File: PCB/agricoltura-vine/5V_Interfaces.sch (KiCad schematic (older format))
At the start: 13 parts, among them T19 TSW-108-07-G-T, T20 TSW-108-07-G-T, U8 SN74LV541APWR, U9 TXB0108PWR

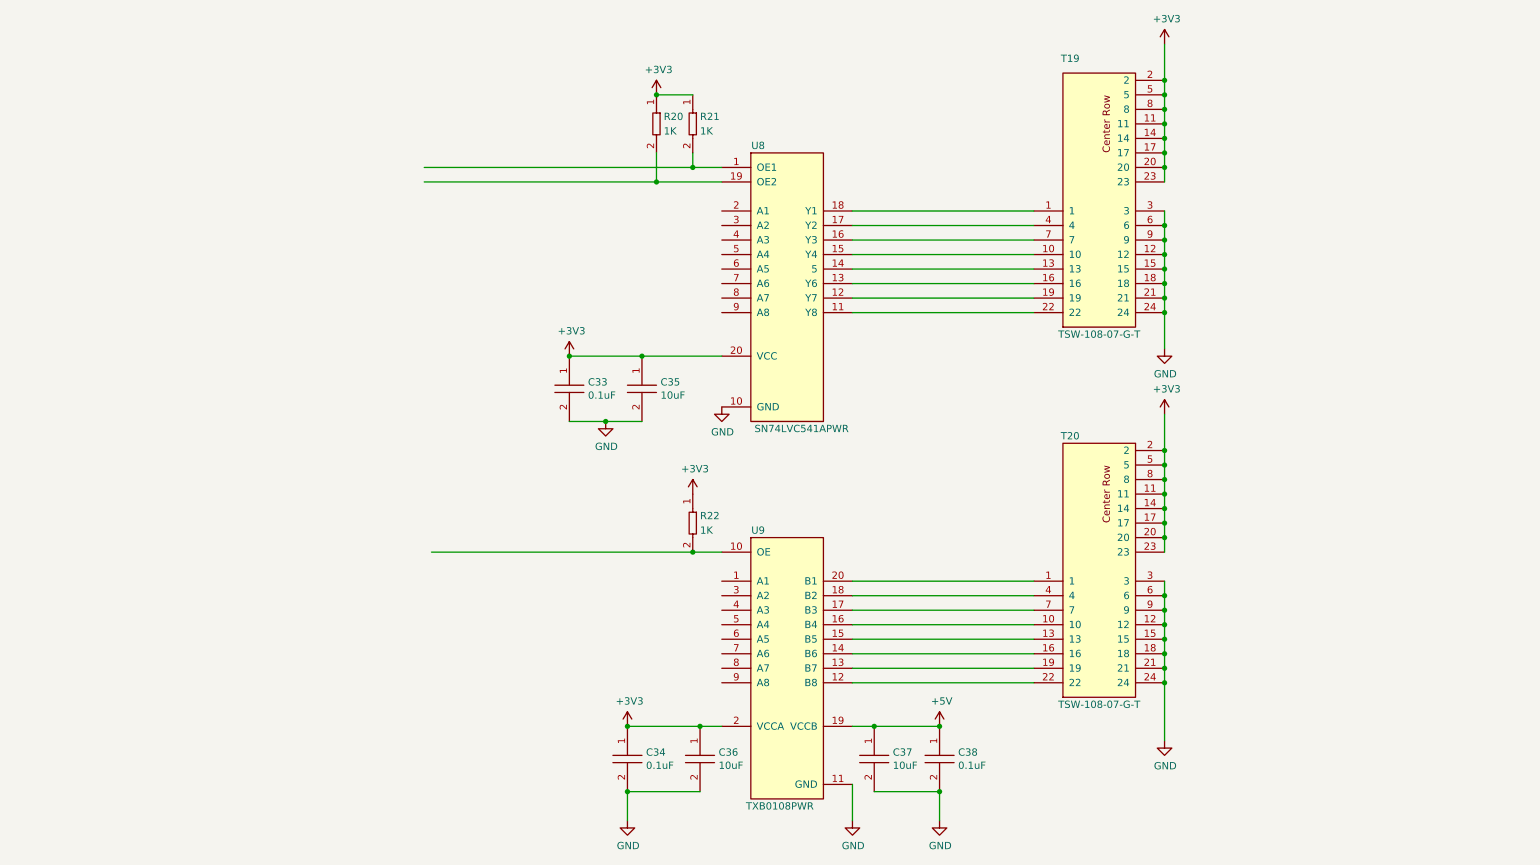
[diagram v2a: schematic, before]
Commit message: Board shape and Rough PLacement
Board shape adjusted to have smaller rounded corners increasing usable space of board shape. Finished rough placement of all the components, no routing yet. Debating connector style and form factor. Right now supports Seeedstudio grove connectors, contemplating Sparkfun Qwiic  and Adafruit Stemma connectors as alternatives or including a variety of all 3.
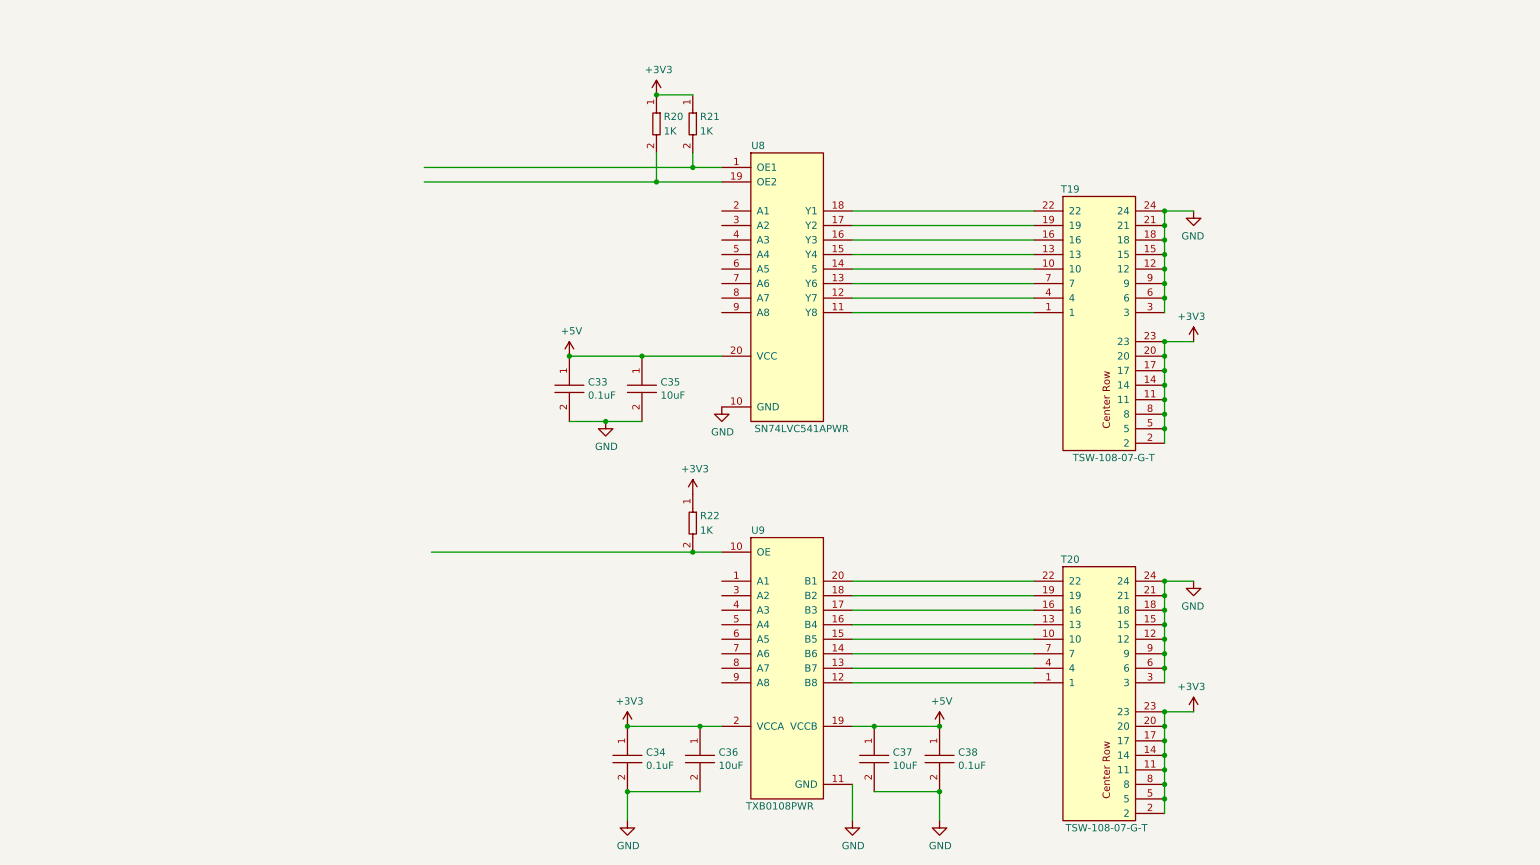
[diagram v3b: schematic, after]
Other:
- moved on the sheet: T19

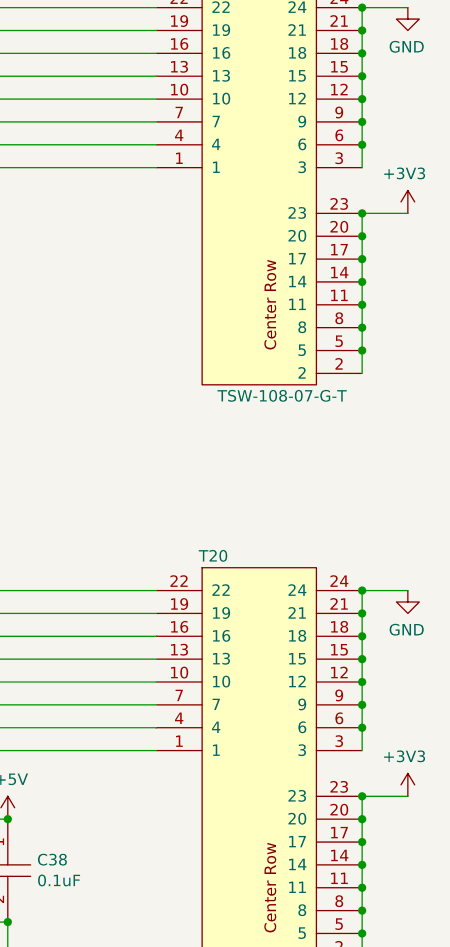
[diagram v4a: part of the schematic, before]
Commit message: Routing and New RS485
swapped over the RS485 chip to a new one and started routing the board.
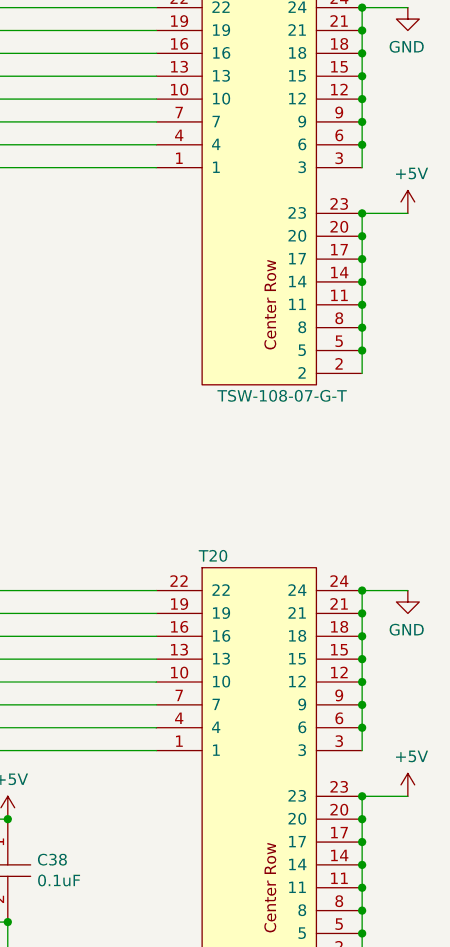
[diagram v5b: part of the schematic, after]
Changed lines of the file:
@@
 Wire Wire Line
 	8350 2000 8350 2100
-$Comp
-L power:+3V3 #PWR060
-U 1 1 5F0FF4C1
-P 8550 2900
-F 0 "#PWR060" H 8550 2750 50  0001 C CNN
-F 1 "+3V3" H 8565 3073 50  0000 C CNN
-F 2 "" H 8550 2900 50  0001 C CNN
-F 3 "" H 8550 2900 50  0001 C CNN
-	1    8550 2900
-	-1   0    0    -1
-$EndComp
 Wire Wire Line
 	8350 3600 8350 3500
@@
 Wire Wire Line
 	8350 4550 8350 4650
-$Comp
-L power:+3V3 #PWR0102
-U 1 1 5EF0C7CF
-P 8550 5450
-F 0 "#PWR0102" H 8550 5300 50  0001 C CNN
-F 1 "+3V3" H 8565 5623 50  0000 C CNN
-F 2 "" H 8550 5450 50  0001 C CNN
-F 3 "" H 8550 5450 50  0001 C CNN
-	1    8550 5450
-	-1   0    0    -1
-$EndComp
 Wire Wire Line
 	8350 6150 8350 6050
@@
 $EndComp
 Connection ~ 4250 3000
+$Comp
+L power:+5V #PWR0112
+U 1 1 5F083515
+P 8550 5450
+F 0 "#PWR0112" H 8550 5300 50  0001 C CNN
+F 1 "+5V" H 8565 5623 50  0000 C CNN
+F 2 "" H 8550 5450 50  0001 C CNN
+F 3 "" H 8550 5450 50  0001 C CNN
+	1    8550 5450
+	1    0    0    -1
+$EndComp
+$Comp
+L power:+5V #PWR0113
+U 1 1 5F08769B
+P 8550 2900
+F 0 "#PWR0113" H 8550 2750 50  0001 C CNN
+F 1 "+5V" H 8565 3073 50  0000 C CNN
+F 2 "" H 8550 2900 50  0001 C CNN
+F 3 "" H 8550 2900 50  0001 C CNN
+	1    8550 2900
+	1    0    0    -1
+$EndComp
 $EndSCHEMATC

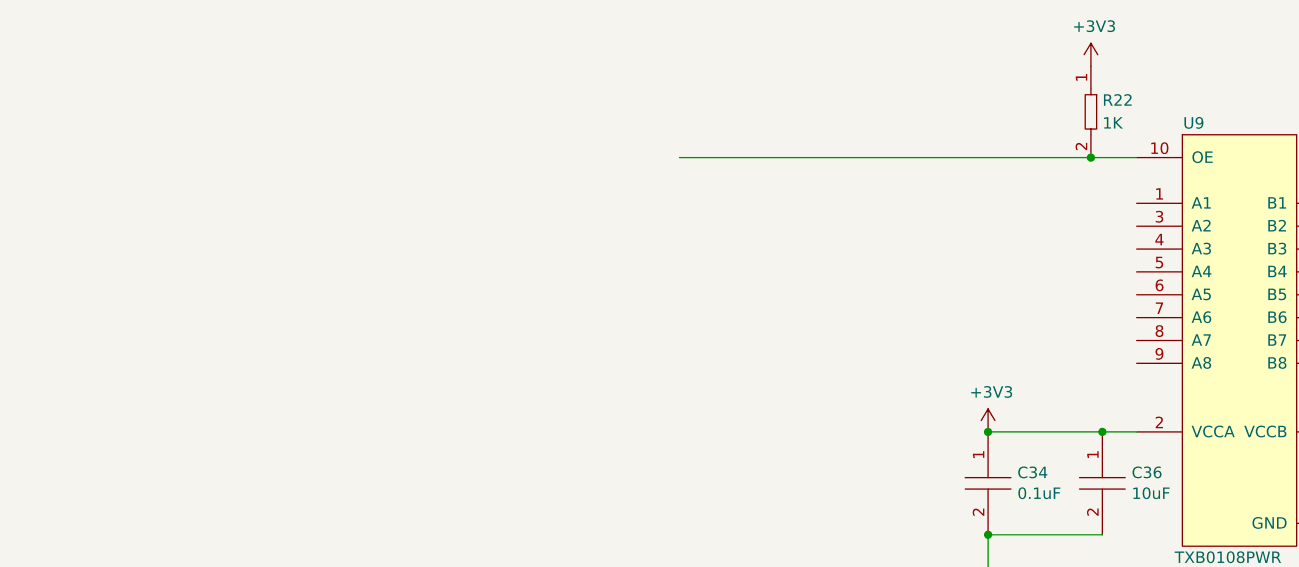
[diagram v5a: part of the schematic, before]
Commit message: Majopr Progress
Board shape enlarged to simplify layout and accomodate larger size parts for sisterboard like Ivy. QWIIC connectors flipped to be correct, signals were oriented incorrectly in past revisions.
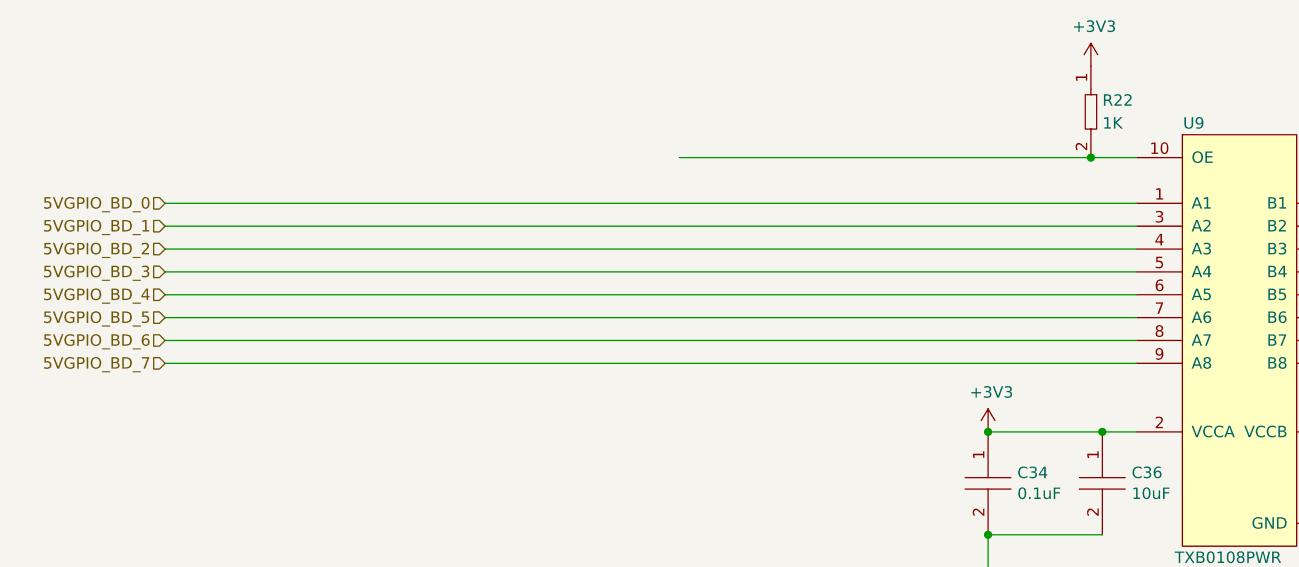
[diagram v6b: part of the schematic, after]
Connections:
- net labels added: 5VGPIO_BD_0, 5VGPIO_BD_1, 5VGPIO_BD_2, 5VGPIO_BD_3, 5VGPIO_BD_4, 5VGPIO_BD_5, 5VGPIO_BD_6, 5VGPIO_BD_7
- wire segments 70 -> 78
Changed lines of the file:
@@
 	1    0    0    -1
 $EndComp
+Text HLabel 1050 4550 0    50   Input ~ 0
+5VGPIO_BD_0
+Text HLabel 1050 4650 0    50   Input ~ 0
+5VGPIO_BD_1
+Text HLabel 1050 4750 0    50   Input ~ 0
+5VGPIO_BD_2
+Text HLabel 1050 4850 0    50   Input ~ 0
+5VGPIO_BD_3
+Text HLabel 1050 4950 0    50   Input ~ 0
+5VGPIO_BD_4
+Text HLabel 1050 5050 0    50   Input ~ 0
+5VGPIO_BD_5
+Text HLabel 1050 5150 0    50   Input ~ 0
+5VGPIO_BD_6
+Text HLabel 1050 5250 0    50   Input ~ 0
+5VGPIO_BD_7
+Wire Wire Line
+	1050 4550 5300 4550
+Wire Wire Line
+	5300 4650 1050 4650
+Wire Wire Line
+	1050 4750 5300 4750
+Wire Wire Line
+	5300 4850 1050 4850
+Wire Wire Line
+	5300 5050 1050 5050
+Wire Wire Line
+	1050 4950 5300 4950
+Wire Wire Line
+	1050 5150 5300 5150
+Wire Wire Line
+	1050 5250 5300 5250
 $EndSCHEMATC

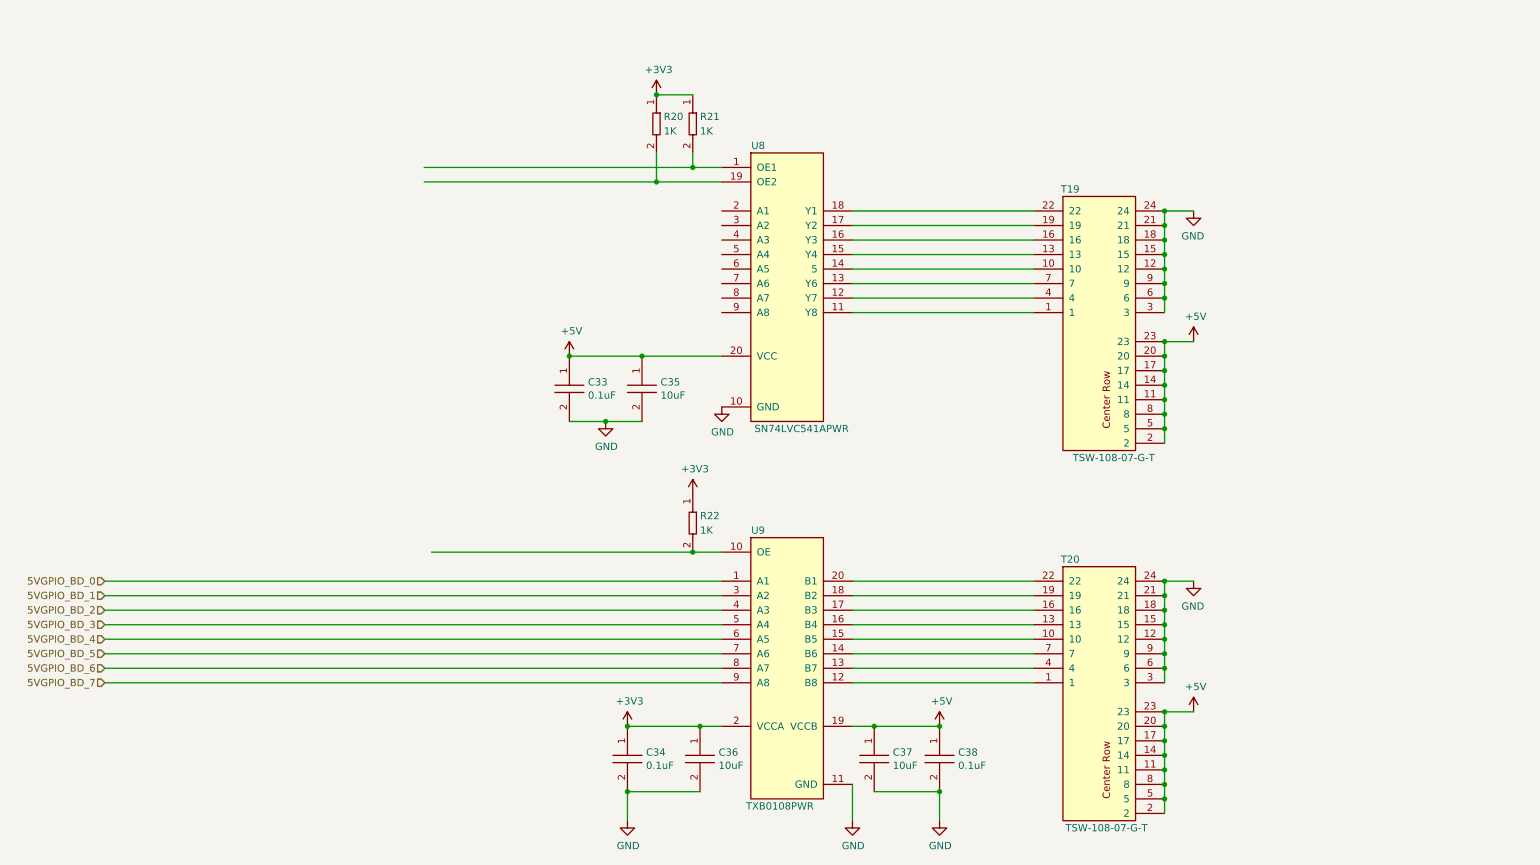
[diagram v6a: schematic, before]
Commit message: IO Expander
added IO expander for 5V IOs
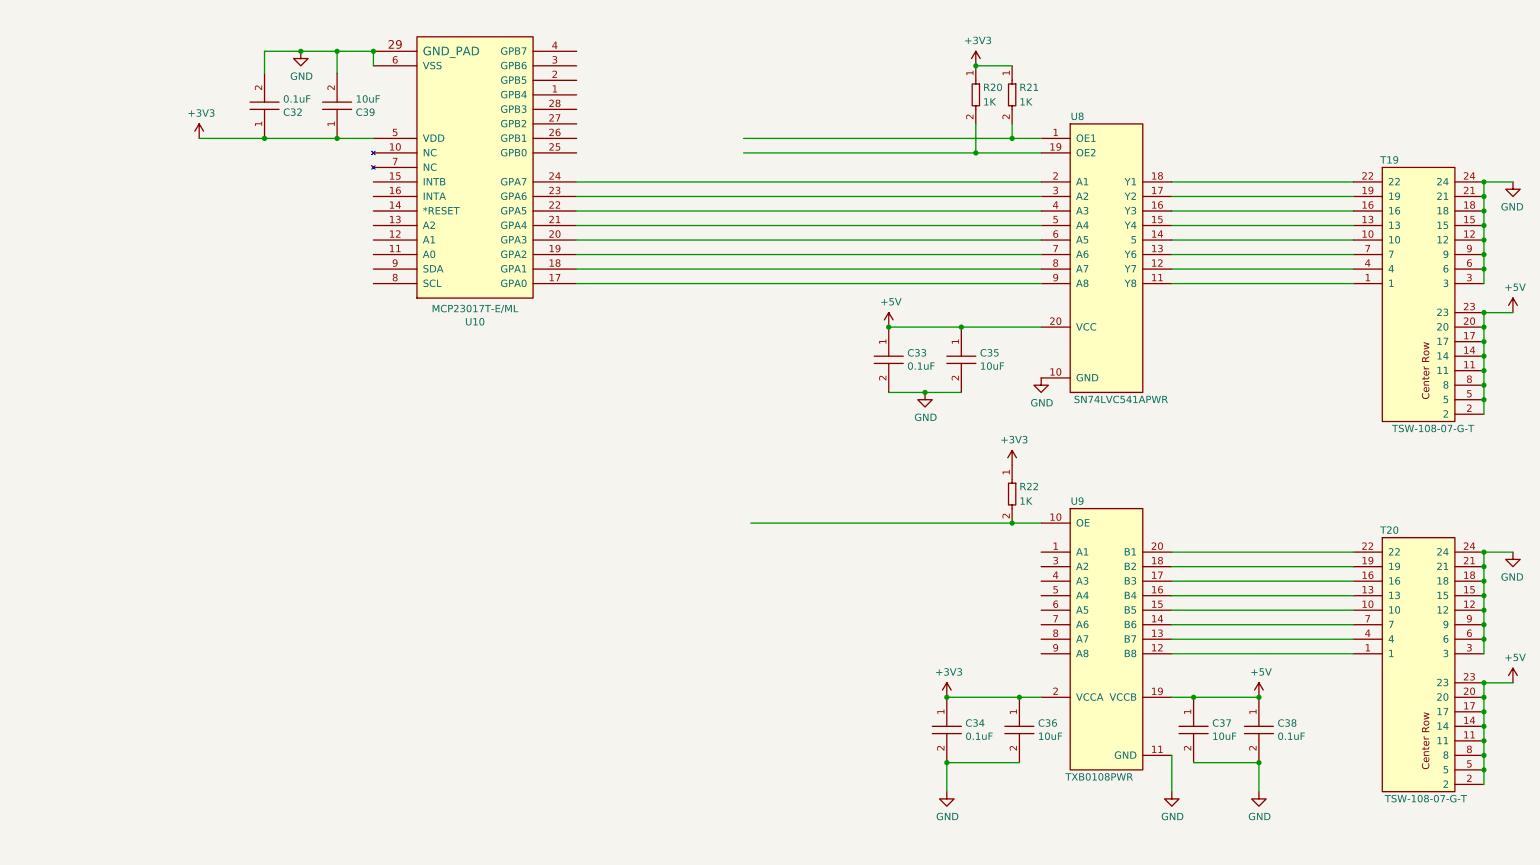
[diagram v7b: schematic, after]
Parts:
- added C32: C0402C104K9PACTU, AVR-KiCAD-Lib-Resistors:R0402, symbol AVR-KiCAD-Lib-Capacitors:C0402C104K9PACTU
- added C39: GRM188R61A106KE69J, AVR-KiCAD-Lib-Capacitors:C0603, symbol AVR-KiCAD-Lib-Capacitors:GRM188R61A106KE69J
- added U10: MCP23017T-E_ML, AVR-KiCAD-Lib-ICs:MCP23017T-E, symbol AVR-KiCAD-Lib-ICs:MCP23017T-E_ML
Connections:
- net labels removed: 5VGPIO_BD_0, 5VGPIO_BD_1, 5VGPIO_BD_2, 5VGPIO_BD_3, 5VGPIO_BD_4, 5VGPIO_BD_5, 5VGPIO_BD_6, 5VGPIO_BD_7
- wire segments 78 -> 87
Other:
- moved on the sheet: C33, C34, C35, C36, C37, C38, R20, R21, R22, T19, T20, U8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
